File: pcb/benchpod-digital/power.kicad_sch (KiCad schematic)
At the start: 70 parts, among them J4 Screw_Terminal_01x02, J5 Screw_Terminal_01x02, J6 Screw_Terminal_01x02, U26 TPS259470ARPWR, U27 TPS259470ARPWR, U29 INA226AIDGSR, U30 TPS82130SILR, U31 AP2112K-1.2, U32 AP2112K-2.5TRG1, U33 INA226AIDGSR, U52 AP2112K-1.8TRG1, U56 TCA9554PWR

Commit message: digital v3r3: carry over the analog v3r2 schematic changes
Same refs and nets as analog v3r1 in these areas, so the v3r2 fixes map 1:1.

- RoHS: D3 SS34 C8678 -> C3014011, D5 SMAJ20A C41376408 -> C5353170.
- U4 ESP32-C3-MINI-1-H4 (C2934569): the N4 is out of stock at JLC; same
  module, footprint and chip, 105 C rated.
- Package shrinks (whole BOM lines, no new lines): 8.2p C29/C30/C50/C51 and
  3.3n C99/C102/C119/C226 0603 -> 0402, 2.2u C218/C219 1206 -> 0603.
- EMC: D11 spare channels on USB CC1/CC2, U34 spares on +1V8 and LA_VCCIO.
- Debug: H1 (SWD 2x5) and H3 (HEADER1) removed; J10 SWO/NRST/SWCLK/SWDIO and
  J11 USART2_RX/+3V3/GND/USART2_TX 2x2, both DNP; PB3 = SWO, PD5/PD6 = USART2.

Not carried over: the 0.1 % resistors (on analog they only share lines with
the ADC parts) and the R164 revision strap (stays 1k: firmware runs the
digital board as v3). The PCB still needs Update PCB from Schematic.

Co-Authored-By: Claude Opus 5.5 <noreply@anthropic.com>
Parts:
- C102, C119, C99: footprint Capacitor_SMD:C_0603_1608Metric -> Capacitor_SMD:C_0402_1005Metric; LCSC C1613 -> C26404
- D5: LCSC C41376408 -> C5353170; MPN (none) -> SMAJ20A; Manufacturer R+O(宏嘉诚) -> FOSAN
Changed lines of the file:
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@@
 			)
 		)
-		(property "Footprint" "Capacitor_SMD:C_0603_1608Metric"
+		(property "Footprint" "Capacitor_SMD:C_0402_1005Metric"
 			(at 91.1352 83.82 0)
 			(hide yes)
@@
 			)
 		)
-		(property "LCSC" "C1613"
+		(property "LCSC" "C26404"
 			(at 90.17 80.01 0)
 			(hide yes)
@@
 			)
 		)
-		(property "LCSC" "C41376408"
+		(property "LCSC" "C5353170"
 			(at 43.18 187.96 0)
 			(hide yes)
@@
 			)
 		)
-		(property "Manufacturer" "R+O(宏嘉诚)"
+		(property "Manufacturer" "FOSAN"
+			(at 43.18 187.96 0)
+			(hide yes)
+			(show_name no)
+			(do_not_autoplace no)
+			(effects
+				(font
+					(size 1.27 1.27)
+				)
+			)
+		)
+		(property "MPN" "SMAJ20A"
 			(at 43.18 187.96 0)
 			(hide yes)
@@
 			)
 		)
-		(property "Footprint" "Capacitor_SMD:C_0603_1608Metric"
+		(property "Footprint" "Capacitor_SMD:C_0402_1005Metric"
 			(at 98.7552 135.89 0)
 			(hide yes)
@@
 			)
 		)
-		(property "LCSC" "C1613"
+		(property "LCSC" "C26404"
 			(at 97.79 132.08 0)
 			(hide yes)
@@
 			)
 		)
-		(property "Footprint" "Capacitor_SMD:C_0603_1608Metric"
+		(property "Footprint" "Capacitor_SMD:C_0402_1005Metric"
 			(at 261.3152 31.75 0)
 			(hide yes)
@@
 			)
 		)
-		(property "LCSC" "C1613"
+		(property "LCSC" "C26404"
 			(at 260.35 27.94 0)
 			(hide yes)

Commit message: digital v3r3: right-angle, panel-facing parts for the enclosure
Parts from benchpod-private enclosure/design.md (connector choices):
- J1 LA header: shrouded keyed right-angle 2x13 X9555WR-2x13-6TV01
  (C2682221). Pins 1-22 unchanged (same odd/even IDC numbering), 23-26 GND.
- J4/J5/J6 (target in, target out, 5 V out): pluggable right-angle 3.81 mm
  block, black, DB2ERC-3.81-2P-BK (C5259145); the plug ships separately.
- SW1/SW2 reset/boot: side-push TS24CA (C393942), for pinholes in the panel;
  its two mechanical tabs have no pad number.
- LED1: side-view RGB P4-1204RGBWS2-1.5T-A (C2827295). Pin numbers follow
  its datasheet (1 G, 2 B, 3 R, 4 anode); the colors stay on the same
  iCE40 drivers (RGB0 blue, RGB1 green, RGB2 red).

RJ45, USB-C and USB-A are already right-angle; U4 stays until the Wi-Fi
bridge ships. Footprints/3D models imported into libs/lcsc like the others.

Co-Authored-By: Claude Opus 5.5 <noreply@anthropic.com>
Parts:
- J4, J5, J6: value Screw_Terminal_01x02 -> DB2ERC-3.81-2P-BK; footprint lcsc:CONN-TH_2P-P5.00_WJ500V-5.08-2P -> lcsc_footprints:C5259145_CONN-TH_2P-P3.81_DB2ERC-3.81-2P-BK; LCSC C8465 -> C5259145; LCSC Part C8465 -> C5259145; LCSC Part # C8465 -> C5259145; MFR. Part # WJ500V-5.08-2P -> DB2ERC-3.81-2P-BK
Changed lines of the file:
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@@
 			)
 		)
-		(property "Value" "Screw_Terminal_01x02"
+		(property "Value" "DB2ERC-3.81-2P-BK"
 			(at 36.576 186.944 0)
 			(show_name no)
@@
 			)
 		)
-		(property "Footprint" "lcsc:CONN-TH_2P-P5.00_WJ500V-5.08-2P"
+		(property "Footprint" "lcsc_footprints:C5259145_CONN-TH_2P-P3.81_DB2ERC-3.81-2P-BK"
 			(at 26.67 190.5 0)
 			(hide yes)
@@
 			)
 		)
-		(property "Description" "Generic screw terminal, single row, 01x02, script generated (kicad-library-utils/schlib/autogen/connector/)"
+		(property "Description" "Pluggable terminal block, right-angle, 3.81 mm, 2P, black (the plug ships separately)"
 			(at 26.67 190.5 0)
 			(hide yes)
@@
 			)
 		)
-		(property "LCSC Part #" "C8465"
+		(property "LCSC Part #" "C5259145"
 			(at 26.67 190.5 0)
 			(hide yes)
@@
 			)
 		)
-		(property "MFR. Part #" "WJ500V-5.08-2P"
+		(property "MFR. Part #" "DB2ERC-3.81-2P-BK"
 			(at 26.67 190.5 0)
 			(hide yes)
@@
 			)
 		)
-		(property "LCSC" "C8465"
+		(property "LCSC" "C5259145"
 			(at 26.67 190.5 0)
 			(hide yes)
@@
 			)
 		)
-		(property "LCSC Part" "C8465"
+		(property "LCSC Part" "C5259145"
 			(at 26.67 190.5 0)
 			(hide yes)
@@
 			)
 		)
-		(property "Value" "Screw_Terminal_01x02"
+		(property "Value" "DB2ERC-3.81-2P-BK"
 			(at 168.656 84.074 0)
 			(show_name no)
@@
 			)
 		)
-		(property "Footprint" "lcsc:CONN-TH_2P-P5.00_WJ500V-5.08-2P"
+		(property "Footprint" "lcsc_footprints:C5259145_CONN-TH_2P-P3.81_DB2ERC-3.81-2P-BK"
 			(at 180.34 88.9 0)
 			(hide yes)
@@
 			)
 		)
-		(property "Description" "Generic screw terminal, single row, 01x02, script generated (kicad-library-utils/schlib/autogen/connector/)"
+		(property "Description" "Pluggable terminal block, right-angle, 3.81 mm, 2P, black (the plug ships separately)"
 			(at 180.34 88.9 0)
 			(hide yes)
@@
 			)
 		)
-		(property "LCSC Part #" "C8465"
+		(property "LCSC Part #" "C5259145"
 			(at 180.34 88.9 0)
 			(hide yes)
@@
 			)
 		)
-		(property "MFR. Part #" "WJ500V-5.08-2P"
+		(property "MFR. Part #" "DB2ERC-3.81-2P-BK"
 			(at 180.34 88.9 0)
 			(hide yes)
@@
 			)
 		)
-		(property "LCSC" "C8465"
+		(property "LCSC" "C5259145"
 			(at 180.34 88.9 0)
 			(hide yes)
@@
 			)
 		)
-		(property "LCSC Part" "C8465"
+		(property "LCSC Part" "C5259145"
 			(at 180.34 88.9 0)
 			(hide yes)
@@
 			)
 		)
-		(property "Value" "Screw_Terminal_01x02"
+		(property "Value" "DB2ERC-3.81-2P-BK"
 			(at 175.514 134.874 0)
 			(show_name no)
@@
 			)
 		)
-		(property "Footprint" "lcsc:CONN-TH_2P-P5.00_WJ500V-5.08-2P"
+		(property "Footprint" "lcsc_footprints:C5259145_CONN-TH_2P-P3.81_DB2ERC-3.81-2P-BK"
 			(at 179.07 129.54 0)
 			(hide yes)
@@
 			)
 		)
-		(property "Description" "Generic screw terminal, single row, 01x02, script generated (kicad-library-utils/schlib/autogen/connector/)"
+		(property "Description" "Pluggable terminal block, right-angle, 3.81 mm, 2P, black (the plug ships separately)"
 			(at 179.07 129.54 0)
 			(hide yes)
@@
 			)
 		)
-		(property "LCSC Part #" "C8465"
+		(property "LCSC Part #" "C5259145"
 			(at 179.07 129.54 0)
 			(hide yes)
@@
 			)
 		)
-		(property "MFR. Part #" "WJ500V-5.08-2P"
+		(property "MFR. Part #" "DB2ERC-3.81-2P-BK"
 			(at 179.07 129.54 0)
 			(hide yes)
@@
 			)
 		)
-		(property "LCSC" "C8465"
+		(property "LCSC" "C5259145"
 			(at 179.07 129.54 0)
 			(hide yes)
@@
 			)
 		)
-		(property "LCSC Part" "C8465"
+		(property "LCSC Part" "C5259145"
 			(at 179.07 129.54 0)
 			(hide yes)

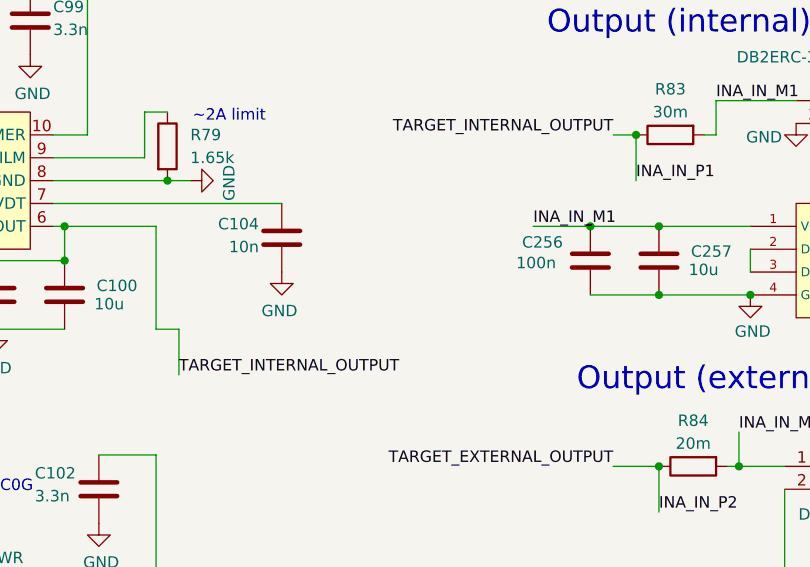
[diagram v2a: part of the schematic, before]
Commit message: digital v3r3: SY6280AAC power switches for module and bridge, TVS on 5 V outputs
- U59 (module 5 V) and U60 (bridge USB-A 5 V) become SY6280AAC (C55136,
  about $0.09) instead of TPS259470 eFuses (about $1 each); 12 support parts
  removed. Current limit 6800/Rset: module 4.7k = about 1.45 A, bridge
  4.7k + 2.2k (R187 + R195) = 6.9k = about 1 A, both from existing BOM lines.
  EN keeps its 10k pull-up (on at power-up), PD10 / PD14 still switch them.
- The FLT/PG flags are gone with the eFuses: PD11, PD12, PD15 and PG2 are free
  again (no-connect), and their four sheet pins are removed.
- SMAJ5.0A TVS (same line as D1): D22 on the bridge USB-A VBUS, D23 on target
  power 1 (USB1/J5).

BOM: one new line (SY6280AAC). The TPS259470 line stays for U26, U27, U57.

Co-Authored-By: Claude Opus 5.5 <noreply@anthropic.com>
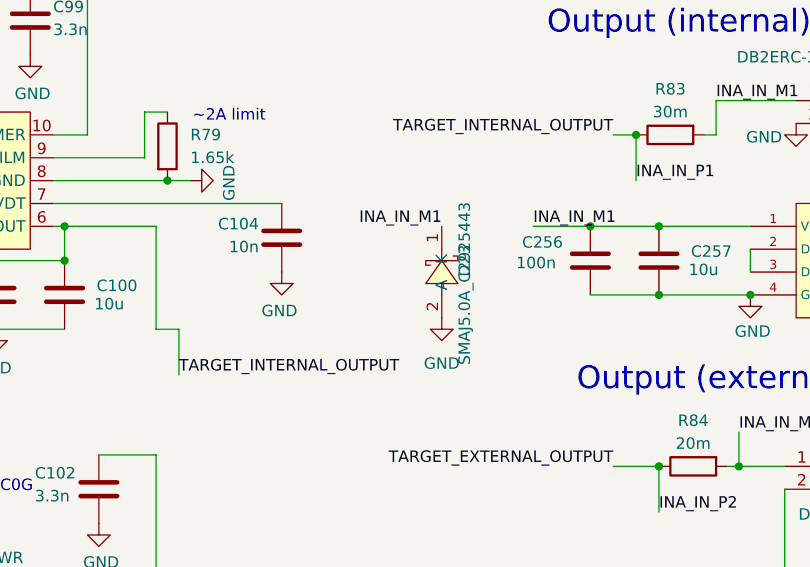
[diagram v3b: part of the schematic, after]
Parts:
- added D23: SMAJ5.0A_C2925443, lcsc:SMA_L4.3-W2.6-LS5.0-RD, symbol lcsc_lib:SMAJ5.0A_C2925443
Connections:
- net GND: now also D23.2 (A)
- net INA_IN_M1: now also D23.1 (K)
